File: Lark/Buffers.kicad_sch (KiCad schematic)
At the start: 5 parts, among them U12 SN74LVC541ARGYR, U13 SN74LVC2G34DBVR

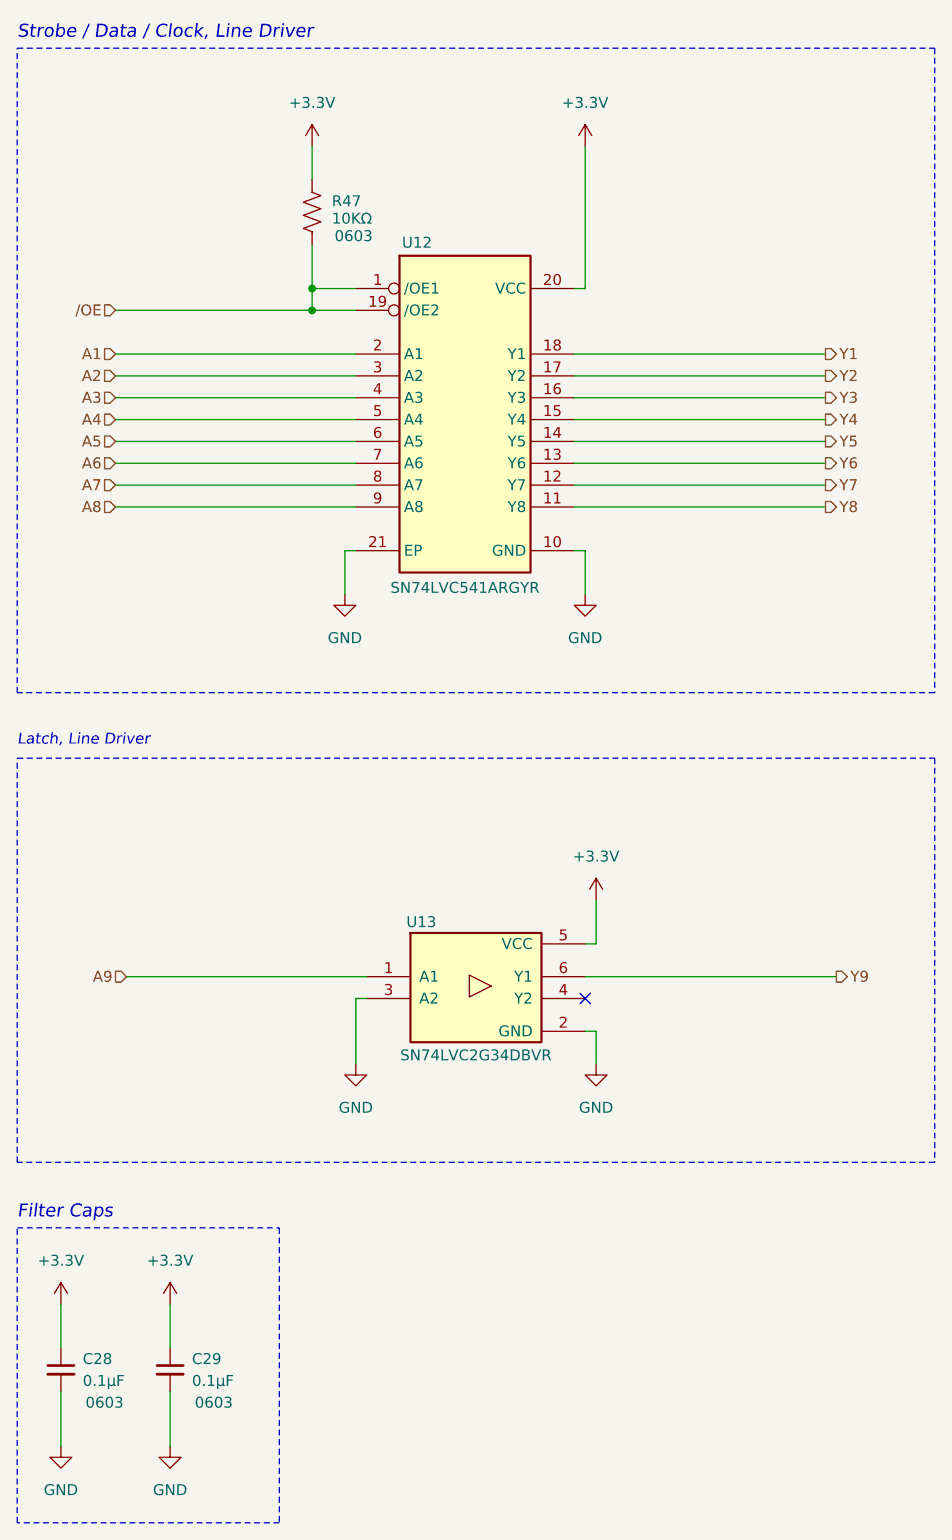
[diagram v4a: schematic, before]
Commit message: updated WIP
- fixed high-side switch (swapped out pfets)
- swapped out bleeder fet.
- changed a few footprints.
- changed zeners to 15v ones
- added soft-start cap back in to the high-side switch.

(today ive mainly been struggling with the inrush current, but I think its solved now)
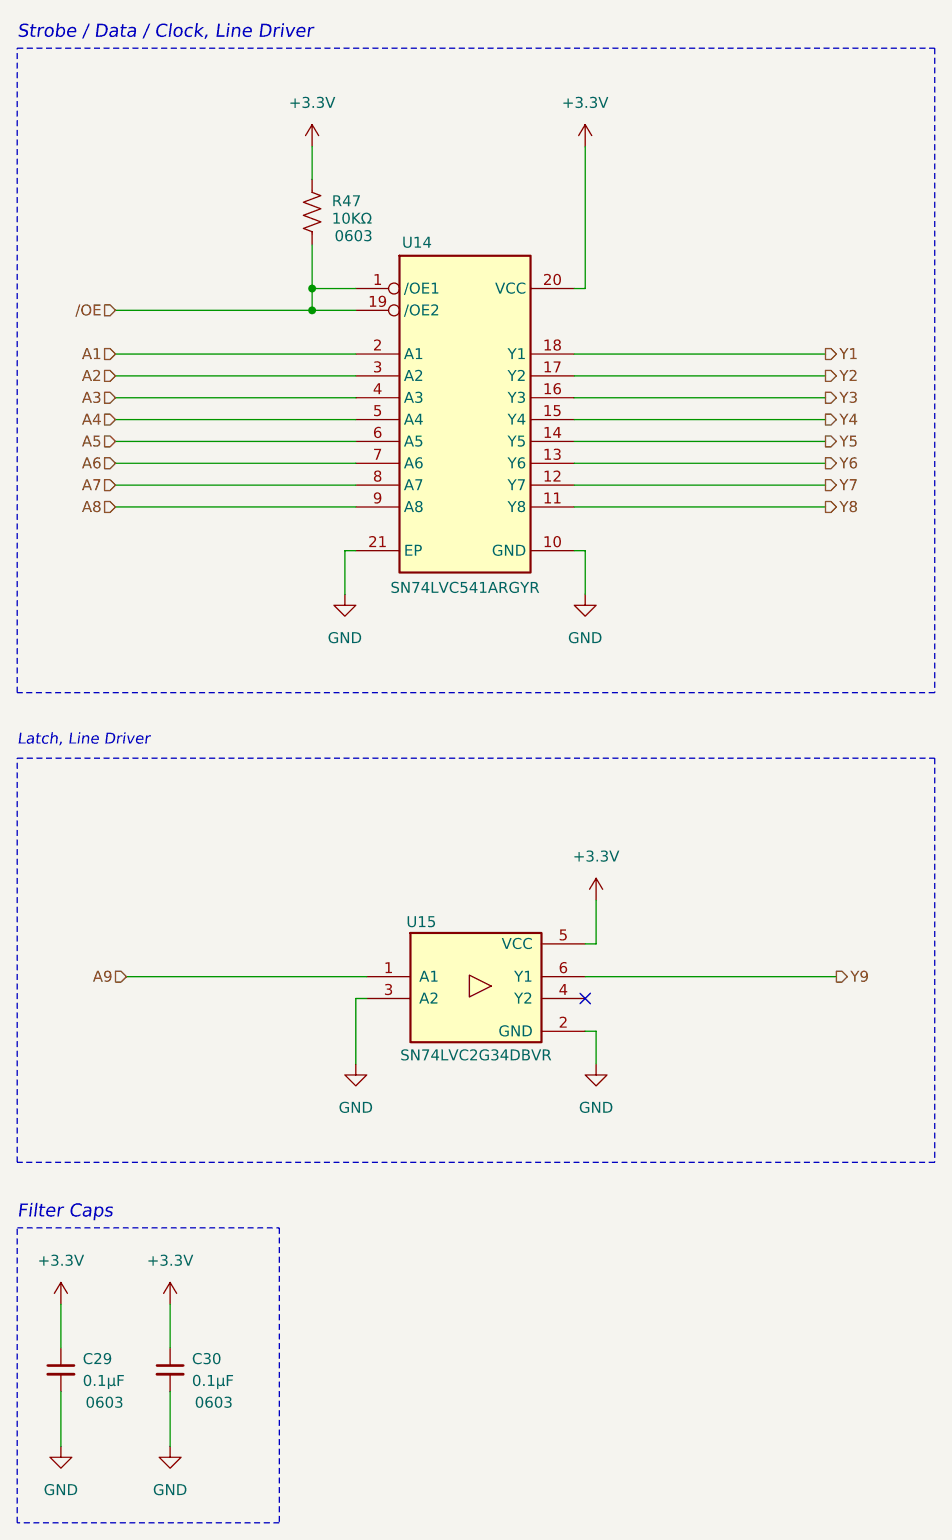
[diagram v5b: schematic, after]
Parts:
- renumbered C28 to C29, C29 to C30, U12 to U14, U13 to U15
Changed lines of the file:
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@@
 		(on_board yes)
 		(dnp no)
-		(property "Reference" "U13"
+		(property "Reference" "U15"
 			(at 64.77 123.19 0)
 			(effects
@@
 			(project ""
 				(path "/a351af57-4353-47da-9f45-7393de572768/6e291d34-e508-4d3b-a2e9-20acfef2b928/cf6d8bd3-7897-4dde-81d8-03d5b6d87e30"
-					(reference "U13")
+					(reference "U15")
 					(unit 1)
 				)
@@
 		(dnp no)
 		(fields_autoplaced yes)
-		(property "Reference" "#PWR0128"
+		(property "Reference" "#PWR0129"
 			(at 85.09 124.46 0)
 			(effects
@@
 			(project "Lark"
 				(path "/a351af57-4353-47da-9f45-7393de572768/6e291d34-e508-4d3b-a2e9-20acfef2b928/cf6d8bd3-7897-4dde-81d8-03d5b6d87e30"
-					(reference "#PWR0128")
+					(reference "#PWR0129")
 					(unit 1)
 				)
@@
 		(dnp no)
 		(fields_autoplaced yes)
-		(property "Reference" "#PWR0134"
+		(property "Reference" "#PWR0135"
 			(at 35.56 190.5 0)
 			(effects
@@
 			(project "Lark"
 				(path "/a351af57-4353-47da-9f45-7393de572768/6e291d34-e508-4d3b-a2e9-20acfef2b928/cf6d8bd3-7897-4dde-81d8-03d5b6d87e30"
-					(reference "#PWR0134")
+					(reference "#PWR0135")
 					(unit 1)
 				)
@@
 		(dnp no)
 		(fields_autoplaced yes)
-		(property "Reference" "#PWR0130"
+		(property "Reference" "#PWR0131"
 			(at 85.09 146.05 0)
 			(effects
@@
 			(project "Lark"
 				(path "/a351af57-4353-47da-9f45-7393de572768/6e291d34-e508-4d3b-a2e9-20acfef2b928/cf6d8bd3-7897-4dde-81d8-03d5b6d87e30"
-					(reference "#PWR0130")
+					(reference "#PWR0131")
 					(unit 1)
 				)
@@
 		(dnp no)
 		(fields_autoplaced yes)
-		(property "Reference" "#PWR0129"
+		(property "Reference" "#PWR0130"
 			(at 57.15 146.05 0)
 			(effects
@@
 			(project "Lark"
 				(path "/a351af57-4353-47da-9f45-7393de572768/6e291d34-e508-4d3b-a2e9-20acfef2b928/cf6d8bd3-7897-4dde-81d8-03d5b6d87e30"
-					(reference "#PWR0129")
+					(reference "#PWR0130")
 					(unit 1)
 				)
@@
 		(dnp no)
 		(fields_autoplaced yes)
-		(property "Reference" "#PWR0133"
+		(property "Reference" "#PWR0134"
 			(at 22.86 190.5 0)
 			(effects
@@
 			(project "Lark"
 				(path "/a351af57-4353-47da-9f45-7393de572768/6e291d34-e508-4d3b-a2e9-20acfef2b928/cf6d8bd3-7897-4dde-81d8-03d5b6d87e30"
-					(reference "#PWR0133")
+					(reference "#PWR0134")
 					(unit 1)
 				)
@@
 		(on_board yes)
 		(dnp no)
-		(property "Reference" "C28"
+		(property "Reference" "C29"
 			(at 25.4 173.9962 0)
 			(effects
@@
 			(project "Lark"
 				(path "/a351af57-4353-47da-9f45-7393de572768/6e291d34-e508-4d3b-a2e9-20acfef2b928/cf6d8bd3-7897-4dde-81d8-03d5b6d87e30"
-					(reference "C28")
+					(reference "C29")
 					(unit 1)
 				)
@@
 		(dnp no)
 		(fields_autoplaced yes)
-		(property "Reference" "#PWR0131"
+		(property "Reference" "#PWR0132"
 			(at 22.86 171.45 0)
 			(effects
@@
 			(project "Lark"
 				(path "/a351af57-4353-47da-9f45-7393de572768/6e291d34-e508-4d3b-a2e9-20acfef2b928/cf6d8bd3-7897-4dde-81d8-03d5b6d87e30"
-					(reference "#PWR0131")
+					(reference "#PWR0132")
 					(unit 1)
 				)
@@
 		(on_board yes)
 		(dnp no)
-		(property "Reference" "C29"
+		(property "Reference" "C30"
 			(at 38.1 173.9962 0)
 			(effects
@@
 			(project "Lark"
 				(path "/a351af57-4353-47da-9f45-7393de572768/6e291d34-e508-4d3b-a2e9-20acfef2b928/cf6d8bd3-7897-4dde-81d8-03d5b6d87e30"
-					(reference "C29")
+					(reference "C30")
 					(unit 1)
 				)
@@
 		(dnp no)
 		(fields_autoplaced yes)
-		(property "Reference" "#PWR0125"
+		(property "Reference" "#PWR0126"
 			(at 83.82 36.83 0)
 			(effects
@@
 			(project "Lark"
 				(path "/a351af57-4353-47da-9f45-7393de572768/6e291d34-e508-4d3b-a2e9-20acfef2b928/cf6d8bd3-7897-4dde-81d8-03d5b6d87e30"
-					(reference "#PWR0125")
+					(reference "#PWR0126")
 					(unit 1)
 				)
@@
 		(dnp no)
 		(fields_autoplaced yes)
-		(property "Reference" "#PWR0124"
+		(property "Reference" "#PWR0125"
 			(at 52.07 36.83 0)
 			(effects
@@
 			(project "Lark"
 				(path "/a351af57-4353-47da-9f45-7393de572768/6e291d34-e508-4d3b-a2e9-20acfef2b928/cf6d8bd3-7897-4dde-81d8-03d5b6d87e30"
-					(reference "#PWR0124")
+					(reference "#PWR0125")
 					(unit 1)
 				)
@@
 		(dnp no)
 		(fields_autoplaced yes)
-		(property "Reference" "#PWR0132"
+		(property "Reference" "#PWR0133"
 			(at 35.56 171.45 0)
 			(effects
@@
 			(project "Lark"
 				(path "/a351af57-4353-47da-9f45-7393de572768/6e291d34-e508-4d3b-a2e9-20acfef2b928/cf6d8bd3-7897-4dde-81d8-03d5b6d87e30"
-					(reference "#PWR0132")
+					(reference "#PWR0133")
 					(unit 1)
 				)
@@
 		(on_board yes)
 		(dnp no)
-		(property "Reference" "U12"
+		(property "Reference" "U14"
 			(at 64.262 44.196 0)
 			(effects
@@
 			(project ""
 				(path "/a351af57-4353-47da-9f45-7393de572768/6e291d34-e508-4d3b-a2e9-20acfef2b928/cf6d8bd3-7897-4dde-81d8-03d5b6d87e30"
-					(reference "U12")
+					(reference "U14")
 					(unit 1)
 				)
@@
 		(dnp no)
 		(fields_autoplaced yes)
-		(property "Reference" "#PWR0127"
+		(property "Reference" "#PWR0128"
 			(at 83.82 91.44 0)
 			(effects
@@
 			(project "Lark"
 				(path "/a351af57-4353-47da-9f45-7393de572768/6e291d34-e508-4d3b-a2e9-20acfef2b928/cf6d8bd3-7897-4dde-81d8-03d5b6d87e30"
-					(reference "#PWR0127")
+					(reference "#PWR0128")
 					(unit 1)
 				)
@@
 		(dnp no)
 		(fields_autoplaced yes)
-		(property "Reference" "#PWR0126"
+		(property "Reference" "#PWR0127"
 			(at 55.88 91.44 0)
 			(effects
@@
 			(project "Lark"
 				(path "/a351af57-4353-47da-9f45-7393de572768/6e291d34-e508-4d3b-a2e9-20acfef2b928/cf6d8bd3-7897-4dde-81d8-03d5b6d87e30"
-					(reference "#PWR0126")
-					(unit 1)
-				)
+					(reference "#PWR0127")
+					(unit 1)
+				)

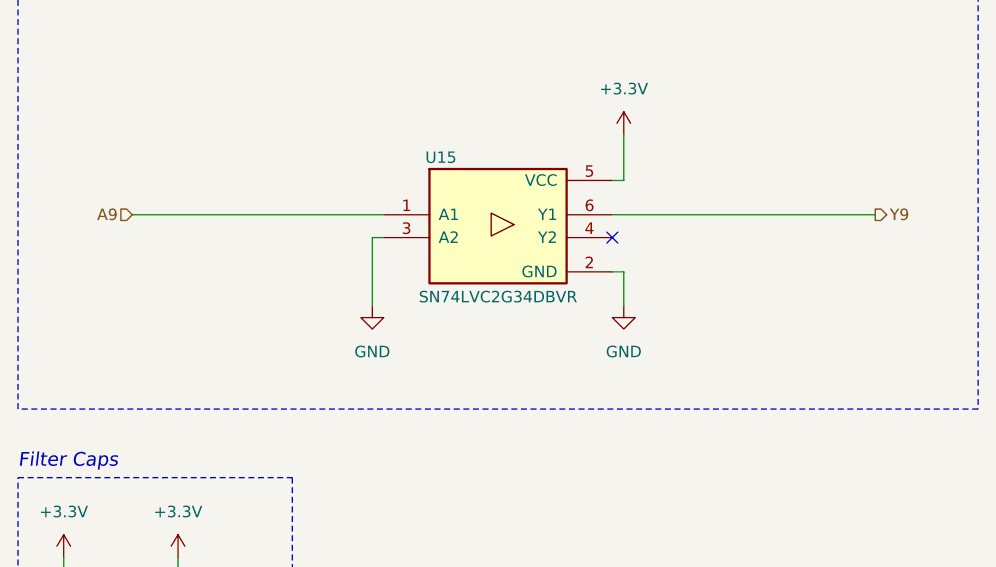
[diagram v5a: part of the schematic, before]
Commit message: started on layout, WIP
I'm not a fan of how its going, I feel like I might redo it, before I get to far into it. A patchy foundation makes an unstable house.
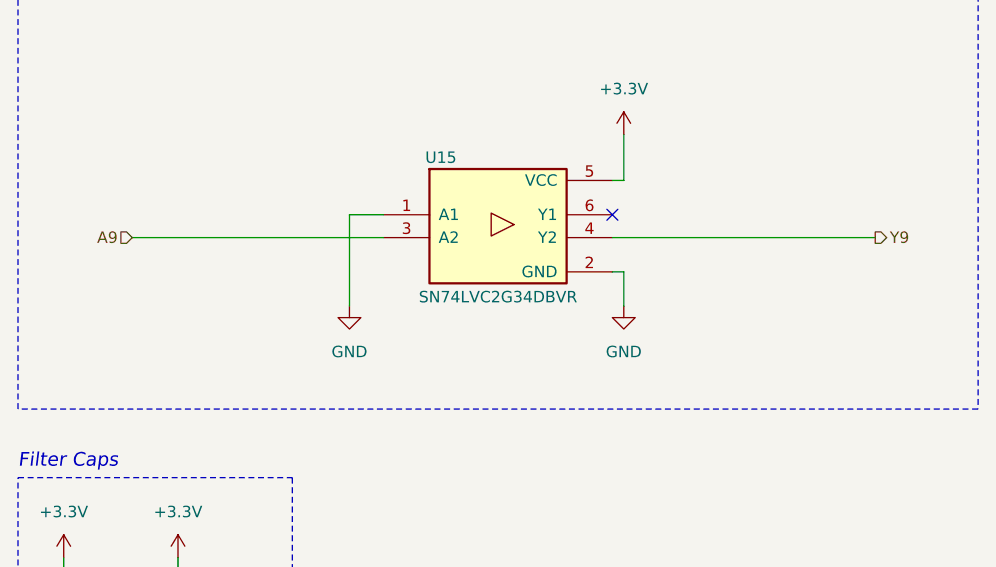
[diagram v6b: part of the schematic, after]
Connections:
- net A9: now also U15.3 (A2); no longer U15.1 (A1)
- net GND: now also U15.1 (A1); no longer U15.3 (A2)
- net Y9: now also U15.4 (Y2); no longer U15.6 (Y1)
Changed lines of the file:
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@@
 	)
 	(no_connect
-		(at 83.82 132.08)
+		(at 83.82 129.54)
 	)
 	(wire
@@
 	(wire
 		(pts
+			(xy 83.82 132.08) (xy 113.03 132.08)
+		)
+		(stroke
+			(width 0)
+			(type default)
+		)
+	)
+	(wire
+		(pts
 			(xy 82.55 67.31) (xy 111.76 67.31)
 		)
@@
 	(wire
 		(pts
+			(xy 54.61 139.7) (xy 54.61 129.54)
+		)
+		(stroke
+			(width 0)
+			(type default)
+		)
+	)
+	(wire
+		(pts
 			(xy 82.55 59.69) (xy 111.76 59.69)
 		)
@@
 	(wire
 		(pts
-			(xy 58.42 132.08) (xy 57.15 132.08)
-		)
-		(stroke
-			(width 0)
-			(type default)
-		)
-	)
-	(wire
-		(pts
-			(xy 57.15 132.08) (xy 57.15 139.7)
-		)
-		(stroke
-			(width 0)
-			(type default)
-		)
-	)
-	(wire
-		(pts
 			(xy 22.86 177.8) (xy 22.86 184.15)
 		)
@@
 	(wire
 		(pts
-			(xy 30.48 129.54) (xy 58.42 129.54)
-		)
-		(stroke
-			(width 0)
-			(type default)
-		)
-	)
-	(wire
-		(pts
 			(xy 85.09 120.65) (xy 85.09 125.73)
 		)
@@
 	(wire
 		(pts
-			(xy 83.82 129.54) (xy 113.03 129.54)
-		)
-		(stroke
-			(width 0)
-			(type default)
-		)
-	)
-	(wire
-		(pts
 			(xy 29.21 72.39) (xy 57.15 72.39)
 		)
@@
 		(pts
 			(xy 83.82 33.02) (xy 83.82 49.53)
+		)
+		(stroke
+			(width 0)
+			(type default)
+		)
+	)
+	(wire
+		(pts
+			(xy 54.61 129.54) (xy 58.42 129.54)
+		)
+		(stroke
+			(width 0)
+			(type default)
+		)
+	)
+	(wire
+		(pts
+			(xy 30.48 132.08) (xy 58.42 132.08)
 		)
 		(stroke
@@
 	(hierarchical_label "A9"
 		(shape input)
-		(at 30.48 129.54 180)
+		(at 30.48 132.08 180)
 		(effects
 			(font
@@
 	(hierarchical_label "Y9"
 		(shape output)
-		(at 113.03 129.54 0)
+		(at 113.03 132.08 0)
 		(effects
 			(font
@@
 	(symbol
 		(lib_id "power:GND")
-		(at 57.15 139.7 0)
+		(at 54.61 139.7 0)
 		(unit 1)
 		(exclude_from_sim no)
@@
 		(fields_autoplaced yes)
 		(property "Reference" "#PWR0130"
-			(at 57.15 146.05 0)
+			(at 54.61 146.05 0)
 			(effects
 				(font
@@
 		)
 		(property "Value" "GND"
-			(at 57.15 144.78 0)
+			(at 54.61 144.78 0)
 			(effects
 				(font
@@
 		)
 		(property "Footprint" ""
-			(at 57.15 139.7 0)
+			(at 54.61 139.7 0)
 			(effects
 				(font
@@
 		)
 		(property "Datasheet" ""
-			(at 57.15 139.7 0)
+			(at 54.61 139.7 0)
 			(effects
 				(font
@@
 		)
 		(property "Description" "Power symbol creates a global label with name \"GND\" , ground"
-			(at 57.15 139.7 0)
-			(effects
-				(font
+			(at 54.61 139.7 0)
+			(effects
+				(font
